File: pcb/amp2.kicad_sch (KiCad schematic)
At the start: 15 parts

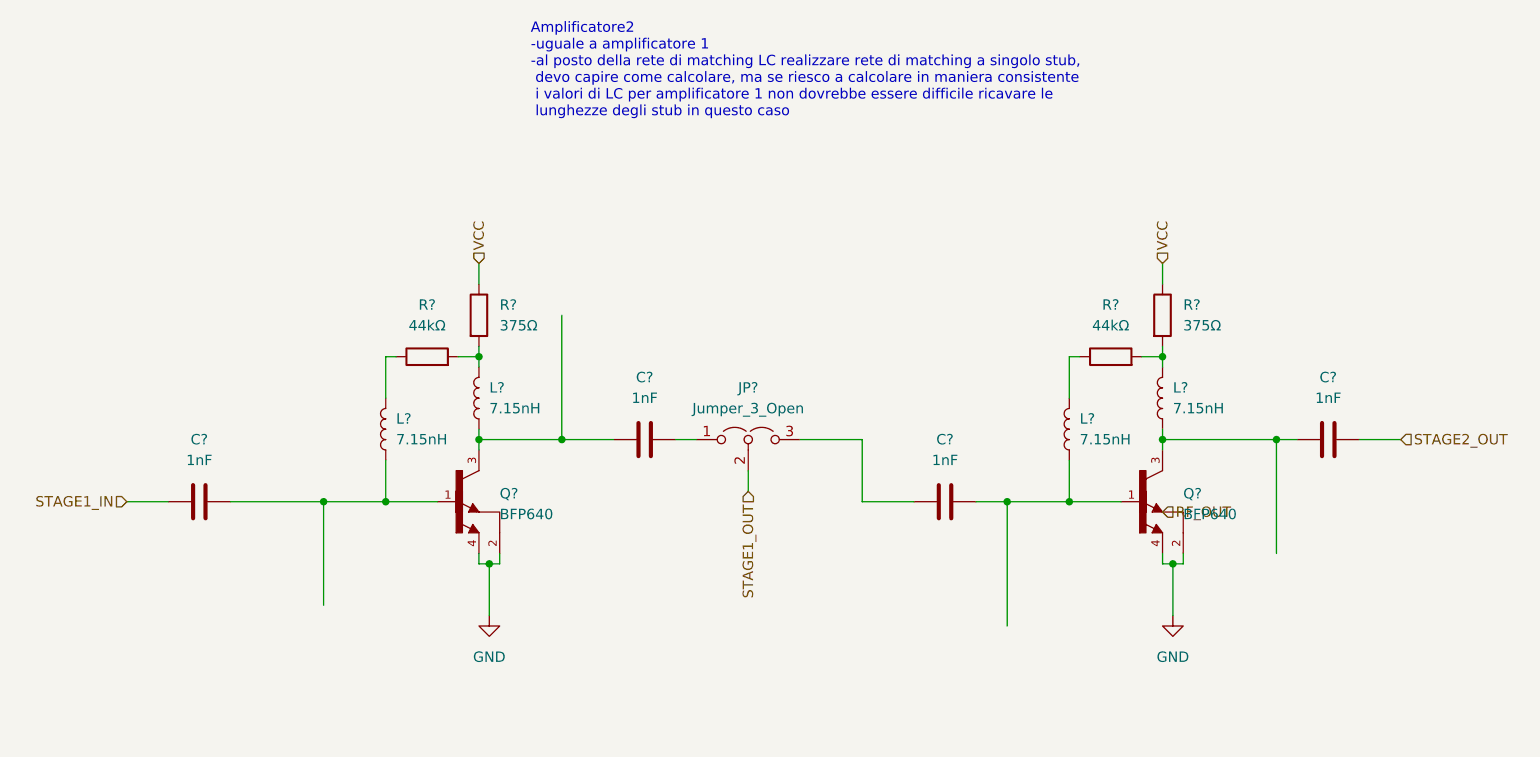
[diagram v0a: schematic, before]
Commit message: Added values for matching network
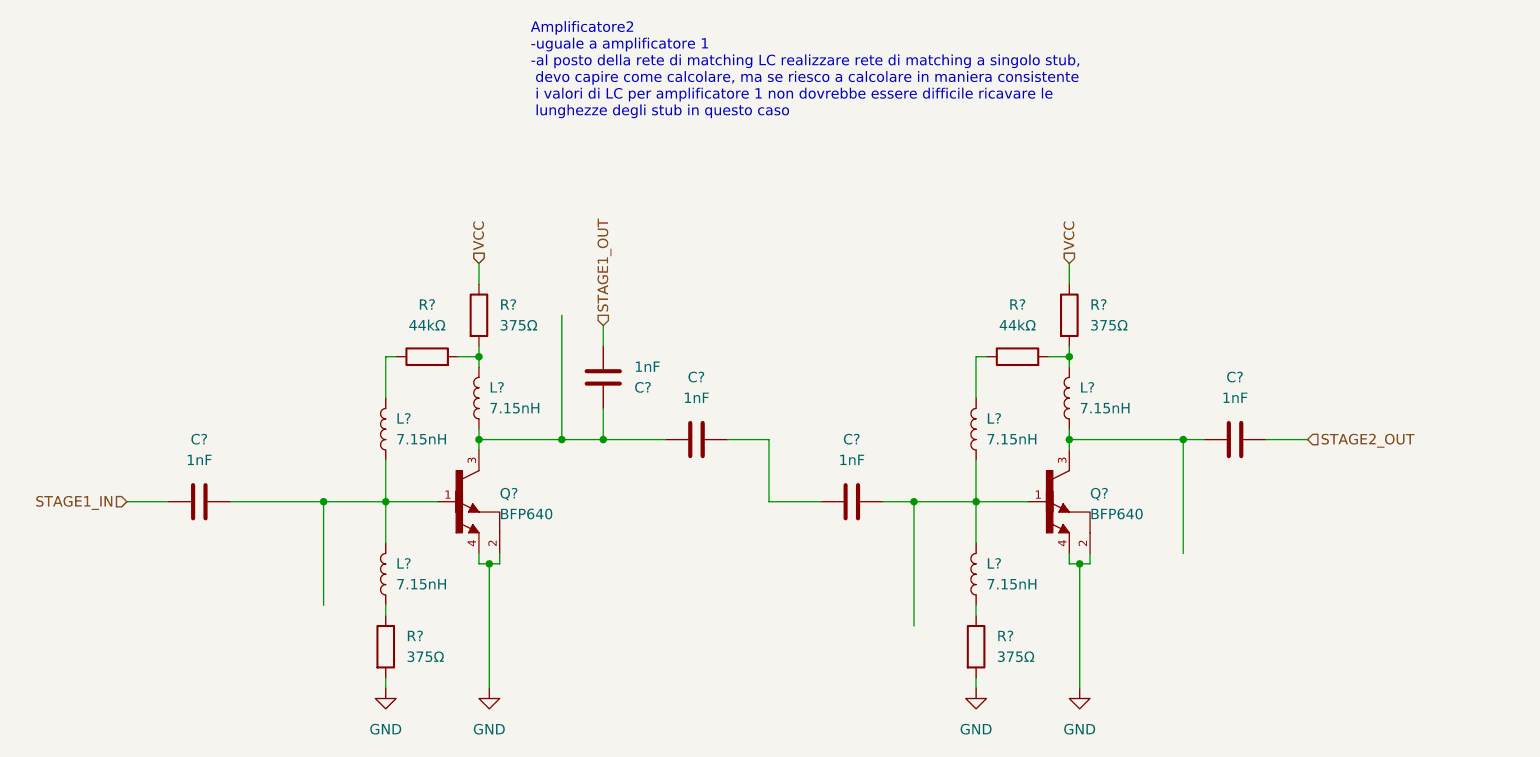
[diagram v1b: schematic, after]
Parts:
- removed JP?: Jumper_3_Open, symbol Jumper:Jumper_3_Open
- added C?: 1nF, symbol Device:C
- added L? (x2): 7.15nH, symbol Device:L
- added R? (x2): 375Ω, symbol Device:R
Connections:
- net GND: now also R?.2, R?.2
- net STAGE1_OUT: now also C?.1
- net at C?.2, L?.1, Q?.1: now also L?.2 (x2)
- net at C?.2: now also C?.1
- net at C?.1, L?.1, Q?.3: now also C?.2
- new net: L?.1, R?.1 (x2)
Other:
- moved on the sheet: C?, L?, Q?, R?

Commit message: Created LTSpice simulation and added suggested fix
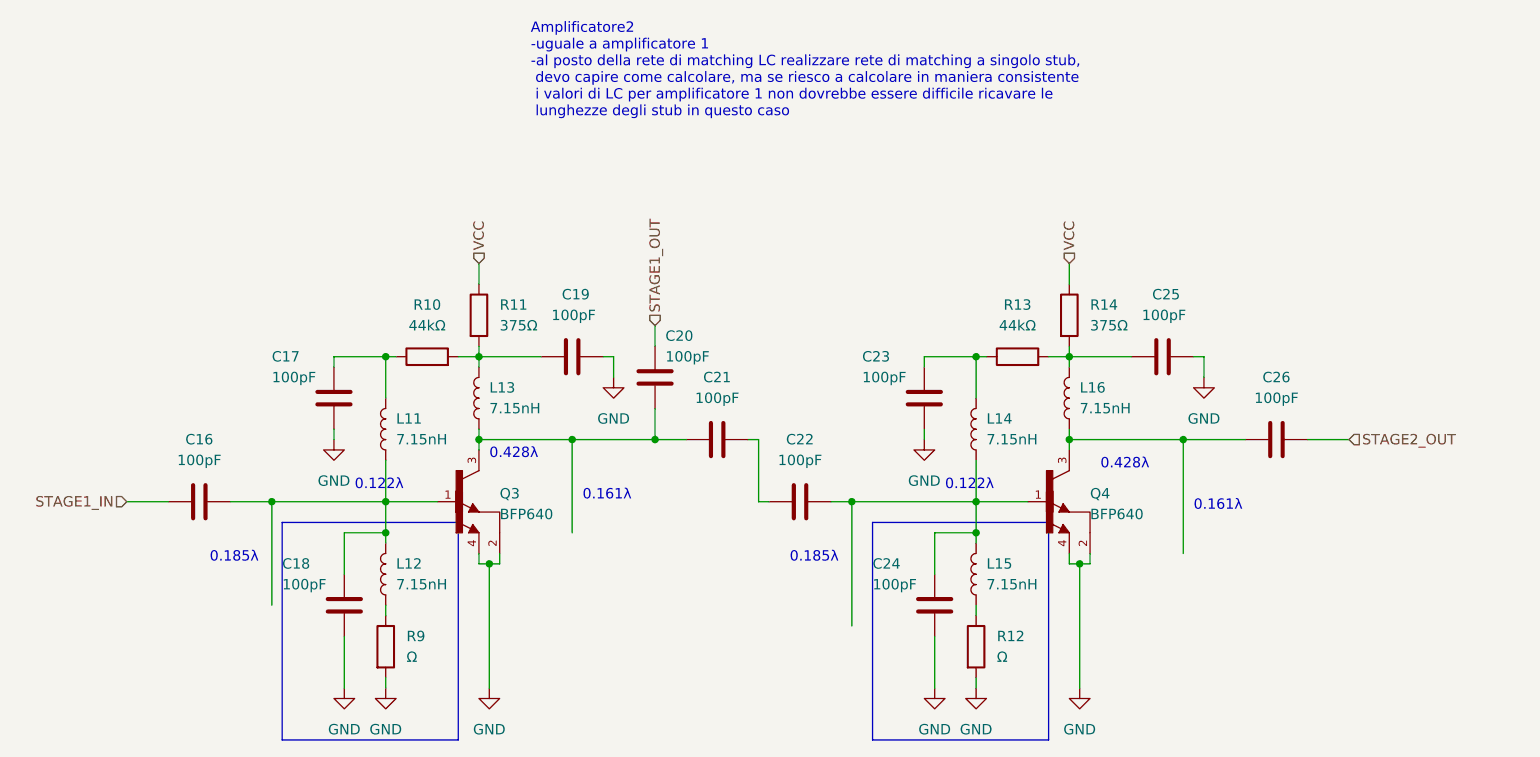
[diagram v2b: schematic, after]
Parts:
- added C17, C18, C19, C23, C24, C25: 100pF, symbol Device:C
- C16, C20, C21, C22, C26: renamed from C?; value 1nF -> 100pF
- R12, R9: renamed from R?; value 375Ω -> Ω
- gave numbers to parts that had none: 12
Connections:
- net GND: now also C17.2, C18.2, C19.2, C23.2, C24.2, C25.2
- net at L14.2, R13.1: now also C23.1
- net at L16.2, R13.2, R14.2: now also C25.1
- net at C22.2, L14.1, L15.2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: now also C24.1
- net at L11.2, R10.1: now also C17.1
- net at L13.2, R10.2, R11.2: now also C19.1
- net at C16.2, L11.1, L12.2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: now also C18.1
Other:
- note added: "0.122λ"
- note added: "0.161λ"
- note added: "0.185λ"
- note added: "0.428λ"
- moved on the sheet: C20, C21, C22, C26

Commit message: Schematic modified as discussed
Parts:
- removed C21, C22, C23, C24, C25, C26: 100pF, symbol Device:C
- removed L16: 7.15nH, symbol Device:L
- removed Q4: BFP640, Nicobigio01:SOT-343, symbol Nicobigio01_Transistor_HBT:BFP640
- removed R13: 44kΩ, symbol Device:R
- removed R14: 375Ω, symbol Device:R
- removed R9: Ω, symbol Device:R
- added C7: 100pF, Capacitor_SMD:C_0603_1608Metric, symbol Device:C
- added C9: 1.45pF, Capacitor_SMD:C_0603_1608Metric, symbol Device:C
- C16, C17, C18, C20: footprint (none) -> Capacitor_SMD:C_0603_1608Metric
- C19: value 100pF -> 398fF; footprint (none) -> Capacitor_SMD:C_0603_1608Metric
- L11: value 7.15nH -> 1.26nH; footprint (none) -> Nicobigio01:Coilcraft_0906-xxLx
- L12, L13, L14: footprint (none) -> Nicobigio01:Coilcraft_1606-xxLx
- L15: value 7.15nH -> 1.78nH; footprint (none) -> Nicobigio01:Coilcraft_0906-xxLx
- R10: value 44kΩ -> Ω; footprint (none) -> Resistor_SMD:R_0603_1608Metric
- R11: value 375Ω -> 44kΩ; footprint (none) -> Resistor_SMD:R_0603_1608Metric
- R12: value Ω -> 375Ω; footprint (none) -> Resistor_SMD:R_0603_1608Metric
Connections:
- net STAGE1_OUT is gone; now on an unnamed net: C20.1
- net GND: now also C16.2, L15.2, R10.2, C9.2; no longer C19.2, R12.2
- net STAGE1_IN: now also C7.1; no longer C16.1
- net STAGE2_OUT: now also C20.2
- net VCC: now also R12.1; no longer R11.1
- net at L14.2: now also C18.1, R11.2, R12.2
- net at L14.1: now also C19.1, Q3.3; no longer L15.2
- net at C17.1, R10.1: now also L13.1; no longer L11.2
- net at L15.1: now also C19.2; no longer R12.1
- net at L12.1: now also L11.2, L13.2, Q3.1
- new net: C7.2, C9.1, L11.1
- new net: C16.1, L12.2, R11.1
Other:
- note removed: "0.122λ"
- note removed: "0.161λ"
- note removed: "0.185λ"
- note removed: "0.428λ"

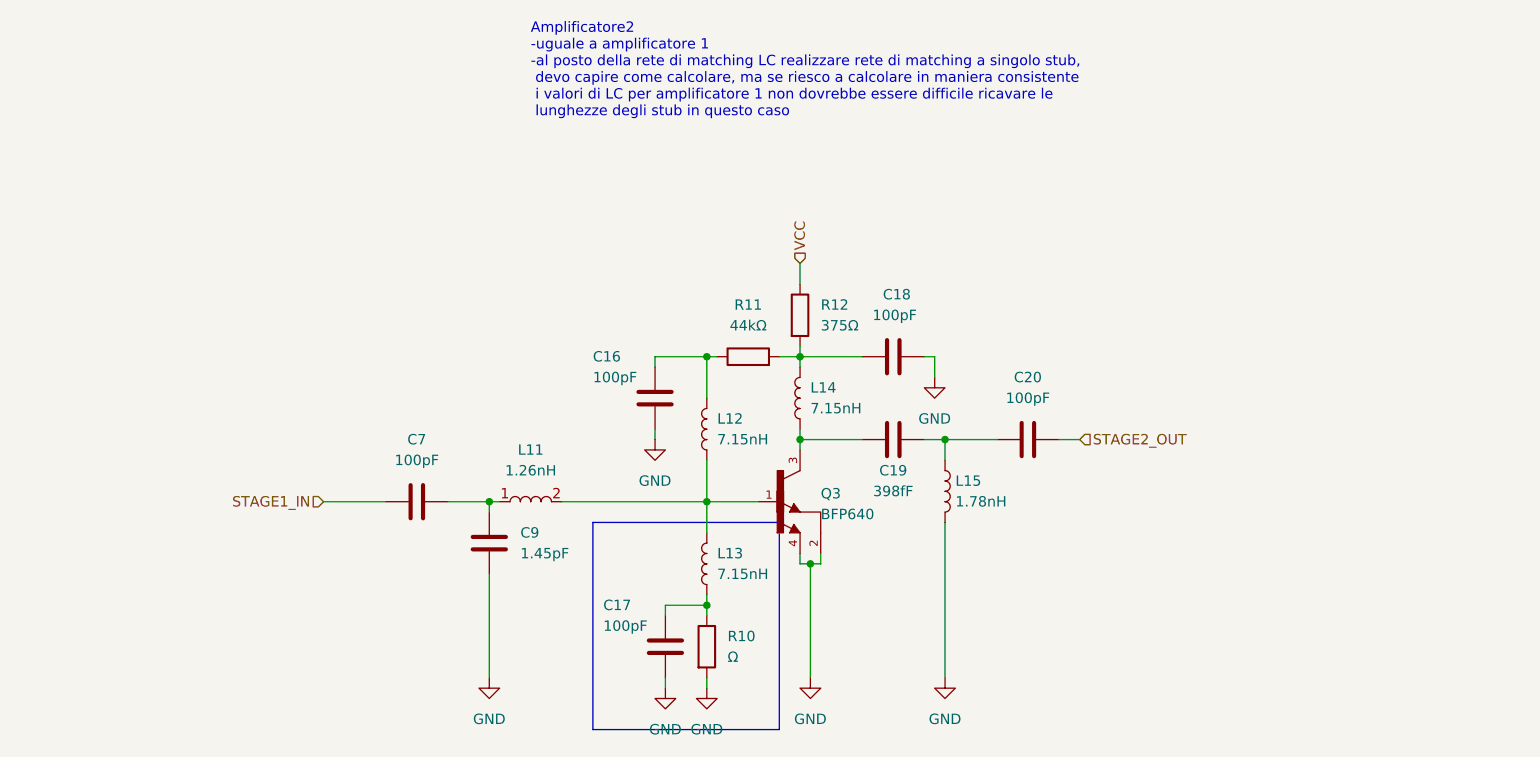
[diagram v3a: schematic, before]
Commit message: Deleted double stage, updated stub stage, L stage and PCB
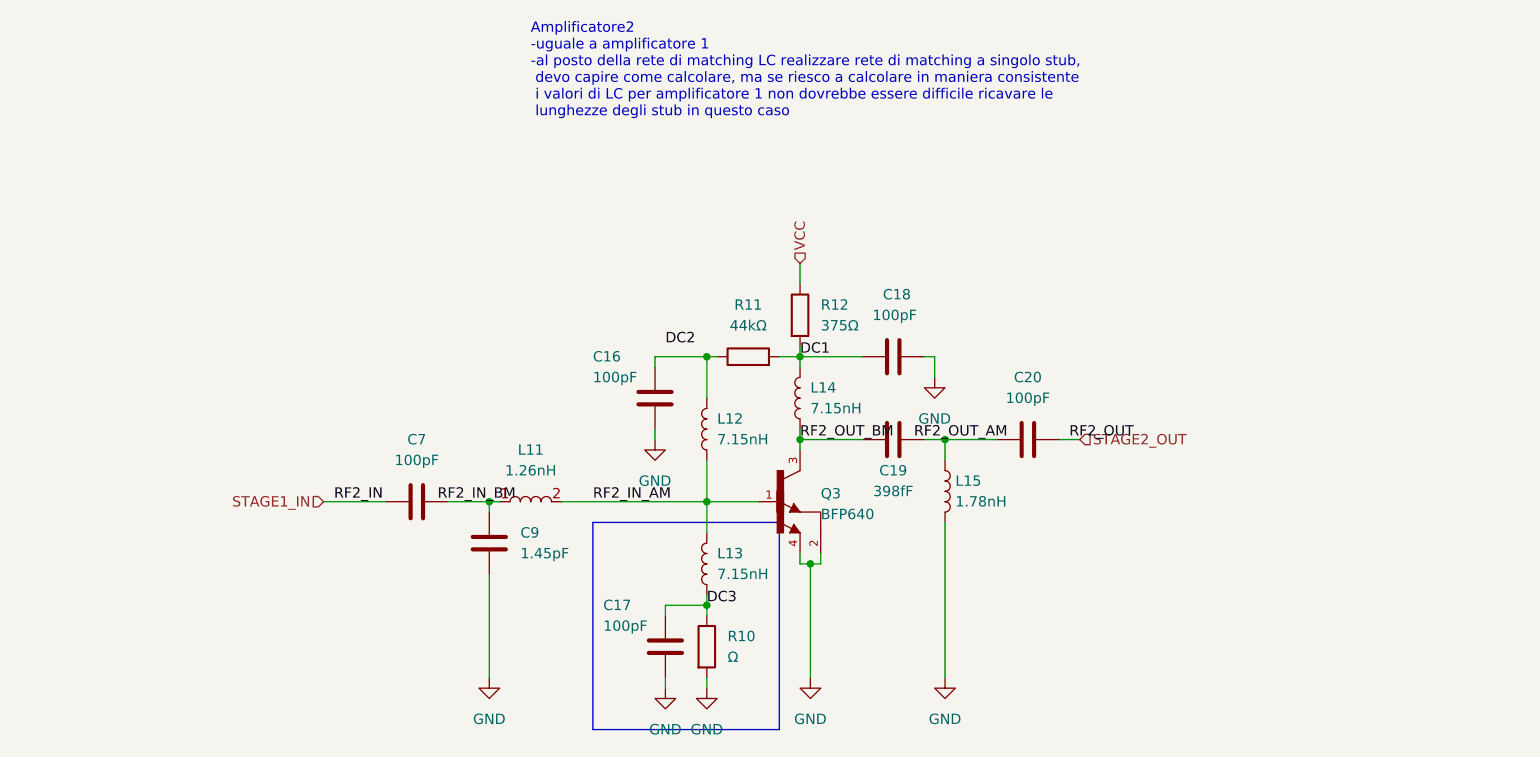
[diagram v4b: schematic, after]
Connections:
- net DC3: now reaches C17.1, L13.1, R10.1
- net RF2_IN_AM: now reaches L11.2, L12.1, L13.2, Q3.1
- net RF2_OUT_BM: now reaches C19.1, L14.1, Q3.3
- net DC1: now reaches C18.1, L14.2, R11.2, R12.2
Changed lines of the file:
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@@
+    (effects (font (size 1.27 1.27)) (justify left bottom))
+  )
+  (label "DC3" (at 146.05 104.14 0)
+    (effects (font (size 1.27 1.27)) (justify left bottom))
+  )
+  (label "RF2_OUT_AM" (at 171.45 83.82 0)
+    (effects (font (size 1.27 1.27)) (justify left bottom))
+  )
+  (label "DC2" (at 140.97 72.39 0)
+    (effects (font (size 1.27 1.27)) (justify left bottom))
+  )
+  (label "RF2_OUT" (at 190.5 83.82 0)
+    (effects (font (size 1.27 1.27)) (justify left bottom))
+  )
+  (label "RF2_IN_BM" (at 113.03 91.44 0)
+    (effects (font (size 1.27 1.27)) (justify left bottom))
+  )
+  (label "RF2_OUT_BM" (at 157.48 83.82 0)
+    (effects (font (size 1.27 1.27)) (justify left bottom))
+  )
+  (label "DC1" (at 157.48 73.66 0)
+    (effects (font (size 1.27 1.27)) (justify left bottom))
+  )
+  (label "RF2_IN_AM" (at 132.08 91.44 0)
+    (effects (font (size 1.27 1.27)) (justify left bottom))
+  )
+  (label "RF2_IN" (at 100.33 91.44 0)
     (effects (font (size 1.27 1.27)) (justify left bottom))
   )

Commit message: Started PCB Layout
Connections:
- net DC1 renamed DC2_1
- net DC3 renamed DC2_3
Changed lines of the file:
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@@
     (effects (font (size 1.27 1.27)) (justify left bottom))
   )
-  (label "DC3" (at 146.05 104.14 0)
+  (label "DC2_3" (at 146.05 104.14 0)
     (effects (font (size 1.27 1.27)) (justify left bottom))
   )
@@
     (effects (font (size 1.27 1.27)) (justify left bottom))
   )
-  (label "DC2" (at 140.97 72.39 0)
+  (label "DC2_2" (at 140.97 72.39 0)
     (effects (font (size 1.27 1.27)) (justify left bottom))
   )
-  (label "RF2_OUT" (at 190.5 83.82 0)
+  (label "RF2_OUT" (at 187.96 83.82 0)
     (effects (font (size 1.27 1.27)) (justify left bottom))
   )
@@
     (effects (font (size 1.27 1.27)) (justify left bottom))
   )
-  (label "DC1" (at 157.48 73.66 0)
+  (label "DC2_1" (at 157.48 73.66 0)
     (effects (font (size 1.27 1.27)) (justify left bottom))
   )
@@
     (pin "4")
   )
-  (symbol (lib_name "L_1") (lib_id "Device:L") (at 124.46 91.44 90) (unit 1)
+  (symbol (lib_id "Device:L") (at 124.46 91.44 90) (unit 1)
     (in_bom yes) (on_board yes) (fields_autoplaced)
     (property "Reference" "L11" (id 0) (at 124.46 85.09 90))
